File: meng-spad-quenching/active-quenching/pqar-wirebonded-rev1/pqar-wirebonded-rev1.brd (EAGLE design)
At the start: 46 x 46 mm, 47 parts, among them IC1 NL17SZ125, IC14 LTC1711, IC17 NL17SZ125, IC2 LTC1711, IC20 NC7WZ16P6X, IC24 TLV272DGK, IC3 NC7SV74K8X, T1 MMBTH10−4LT1G, U1 SN74LVC1G123DCUT, X1 V_A, X2 OUT, X3 V_LOGIC, X4 I_HOLDOFF

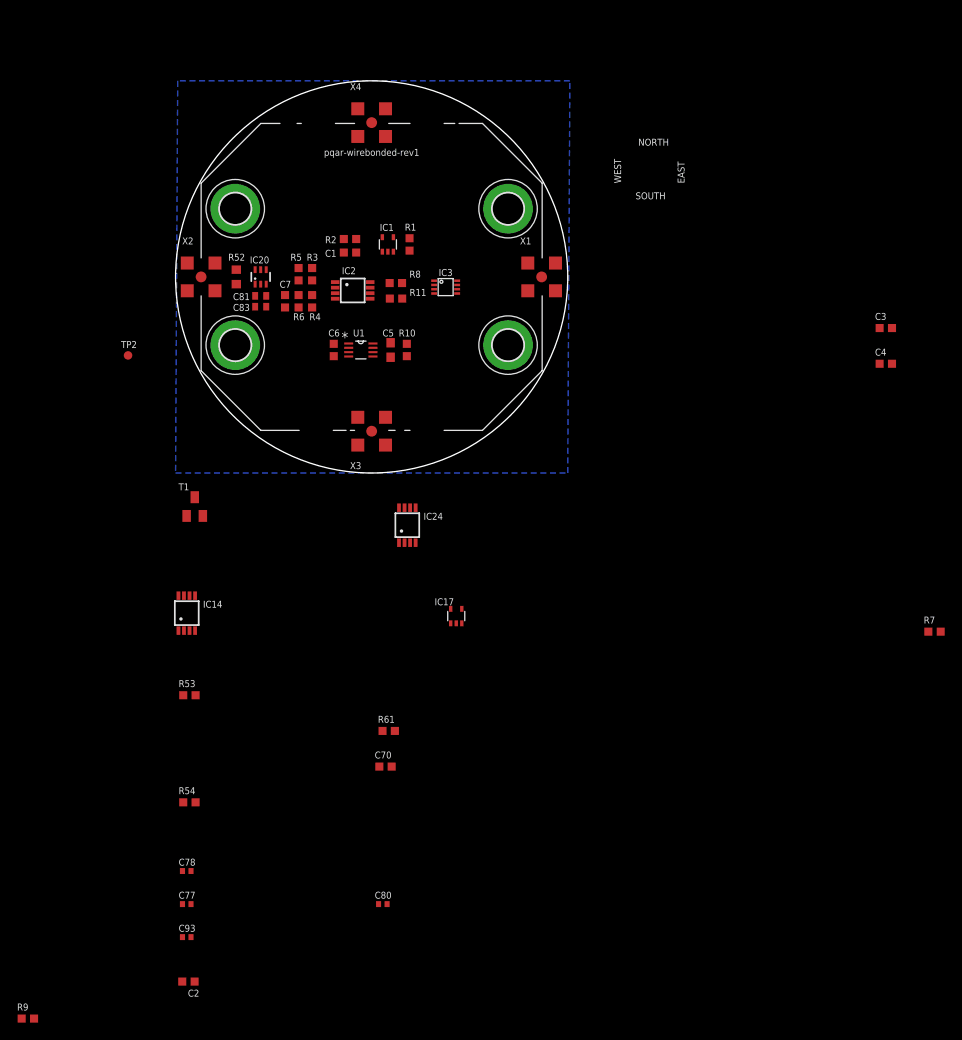
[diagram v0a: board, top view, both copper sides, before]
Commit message: got everything to initially fit on the board
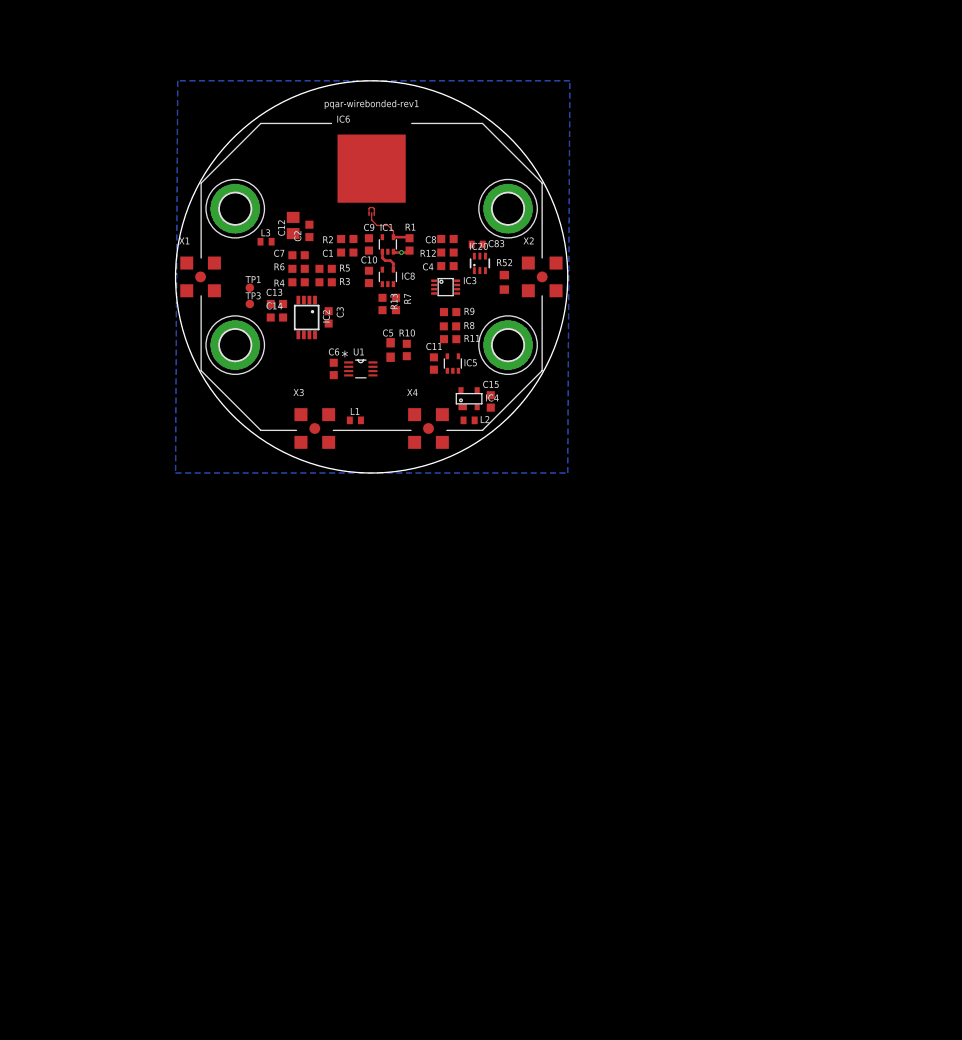
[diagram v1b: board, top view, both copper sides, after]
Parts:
- removed C70: CAP CER 100PF 50V C0G 0603 5%, rcl-modified-footprints:C0603
- removed C77, C80, C93: CAP CER 0.1UF 10V X7R 0402 10%, rcl-modified-footprints:C0402
- removed C78: CAP CER 10000PF 10V X7R 0402 10%, rcl-modified-footprints:C0402
- removed C81: CAP CER 10000PF 10V X7R 0402 10%, rcl:C0402
- removed IC14: LTC1711, meng:MSOP8
- removed IC17: NL17SZ125, 74xx-little-de:SC70-5
- removed IC24: TLV272DGK, meng:MSOP8
- removed R53, R61: RES SMD 220K OHM 1% 1/10W 0603, rcl-modified-footprints:R0603
- removed R54: RES SMD 10K OHM 1% 1/10W 0603, rcl-modified-footprints:R0603
- removed T1: MMBTH10−4LT1G, transistor:SOT23-BEC
- removed TP2: AV_DET, testpad:TP10R
- added C10, C11, C9: IPDiA 935131425610, rcl-modified-footprints:C0603
- added C12: CAP CER 0.1UF 50V X7R 0805 5%, rcl-modified-footprints:C0805
- added C13, C14, C8: DNP, rcl-modified-footprints:C0603
- added C15: CAP CER 0.1UF 50V X7R 0603 5%, rcl-modified-footprints:C0603
- added IC4: BCV62, meng:SOT143B
- added IC5: 74AHC1G14DCK, 74xx-little-us:SC70-5
- added IC6: SPAD-GENERIC, meng:SPAD-WIREBOND-GENERIC-CRYO
- added IC8: 74LVC1G02DCK, 74xx-little-us:SC70-5
- added L1, L2, L3: Samsung CIM05J152NC, meng:R0402
- added R12, R13: RES SMD 0R 0603, rcl-modified-footprints:R0603
- added TP1, TP3: AV_DET, testpad:TP10R
- C2: value CAP CER 100PF 50V C0G 0603 5% -> CAP CER 0.1UF 50V X7R 0603 5%
- R11: value DNP -> RES SMD 0R 0603
- R7: value Vishay FC0603E50R0BTBST1 -> DNP
- moved R9 96.5 mm to (9.21, -4.13)
- moved C2 89.2 mm to (-7.30, 5.40), turned to 90 degrees
- moved R7 73.9 mm to (2.86, -3.17), turned to 270 degrees
- moved C3 65.4 mm to (-5.04, -4.75), turned to 270 degrees
- moved C4 52.7 mm to (8.89, 1.27), turned to 180 degrees
- moved X2 40.0 mm to (20.0, 0.00)
- moved X1 40.0 mm to (-20.1, 0.00)
- moved X4 36.5 mm to (6.67, -17.8)
- moved R52 31.4 mm to (15.6, -0.64)
- moved C83 26.4 mm to (12.4, 3.81), turned to 180 degrees
- moved IC20 25.8 mm to (12.7, 1.59)
- moved R8 8.13 mm to (9.19, -5.80)
- moved R11 7.94 mm to (9.21, -7.30)
- moved X3 6.68 mm to (-6.67, -17.8)
- moved IC2 6.26 mm to (-7.62, -4.76), turned to 180 degrees
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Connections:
- removed net CAP_!RESET: IC17.1
- removed net N$1: C7.1, IC2.2, R5.2, R6.1
- removed net N$11: IC14.3
- removed net N$12: IC20.1, IC20.3, R11.2, U1.5
- removed net N$15: IC14.4
- removed net N$3: C2.1, R2.1, X1.S
- removed net N$4: C1.2, IC2.3, R3.2, R4.1
- removed net N$6: IC3.1, R8.2, R9.2
- removed net NC_RESET: IC3.5
- removed net ONE_SHOT_CAP: C70.1, IC14.2, IC17.4, T1.C
- removed net ONE_SHOT_FB: R53.1, R54.1, T1.E
- removed net ONE_SHOT_VGND: IC24.2, R53.2, R61.1
- removed net PP_N5V0_ANALOG: C80.1, IC24.4, R54.2
- removed net PP_P5V0_ANALOG: C77.1, C78.1, C93.1, IC14.1, IC24.8
- removed net VCC: IC1.5, IC17.5
- removed net VREF_ONE_SHOT_CCS: R61.2
- new net !EN_DRIVER: IC1.1, IC8.4
- new net !QUENCH: IC5.4, R11.2
- new net AV_DET_REF: C13.1, C7.1, IC2.2, R5.2, R6.1
- new net CLK_RESET: IC3.1, R11.1, R8.2, R9.2
- new net DRIVER_IN: IC1.2, IC8.1, R13.1, R7.1
- new net KATHODE_C: C1.2, C14.1, IC2.3, R3.2, R4.1
- new net N$7: C8.1, IC3.6, R12.2
- new net N$8: L2.1, X4.S
- new net QUENCH: IC20.1, IC20.3, IC5.2, R13.2, U1.5
- new net RESET: IC3.5, IC8.2
- new net V_A: L3.1, X1.S
- new net V_A_FILT: C12.1, C2.1, L3.2, R2.1
- net !AV_DET: now also C14.2, TP3.TP
- net !RESET: now also R12.1; no longer IC1.1, IC3.6
- net +5V: now also C10.1, C11.1, C9.1, IC1.5, IC4.3, IC4.4, IC5.5, IC8.5, L1.2; no longer C81.1, IC17.2, X3.S
- net ANODE: now also IC6.A
- net AV_DET: now also C13.2, TP1.TP; no longer TP2.TP
- net GND: now also C10.2, C11.2, C12.2, C15.2, C8.2, C9.2, IC5.3, IC6.GND, IC8.3, R7.2; no longer C70.2, C77.2, C78.2, C80.2, C81.2, C93.2, IC1.2, IC14.5, IC14.6, IC17.3, IC24.3
- net KATHODE: now also IC6.K1, IC6.K2
- net N$17: now also IC4.2
- net N$2: now also C15.1, IC4.1, L2.2; no longer X4.S
- net N$5: now also L1.1, X3.S; no longer IC24.1, T1.B
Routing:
- net ANODE: track 0.00 -> 6.45 mm
- net !EN_DRIVER: track 0.00 -> 3.02 mm
- net GND: track 0.00 -> 2.03 mm, vias 0 -> 1
- net KATHODE: track 0.00 -> 2.00 mm
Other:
- board text removed: "EAST"
- board text removed: "NORTH"
- board text removed: "SOUTH"
- board text removed: "WEST"

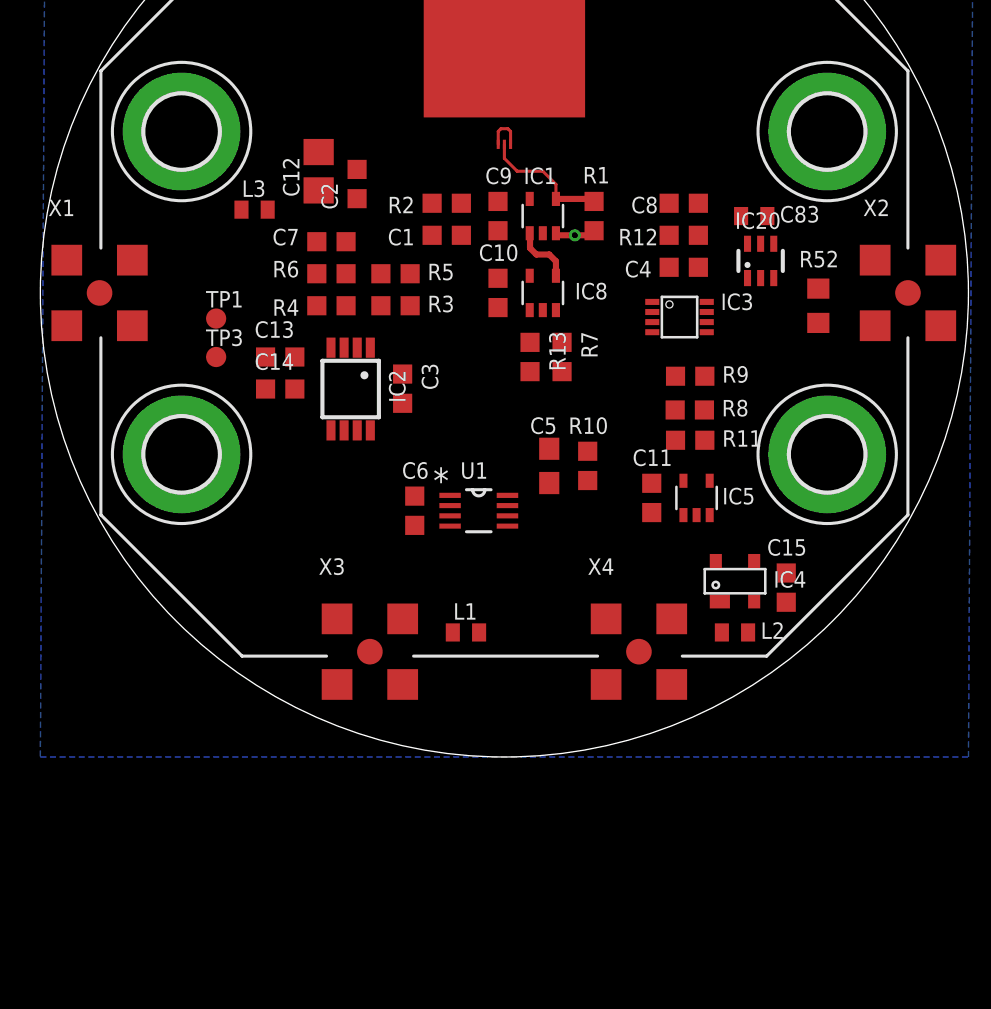
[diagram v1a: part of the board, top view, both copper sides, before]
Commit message: More routing, add or gate for forcing quenching
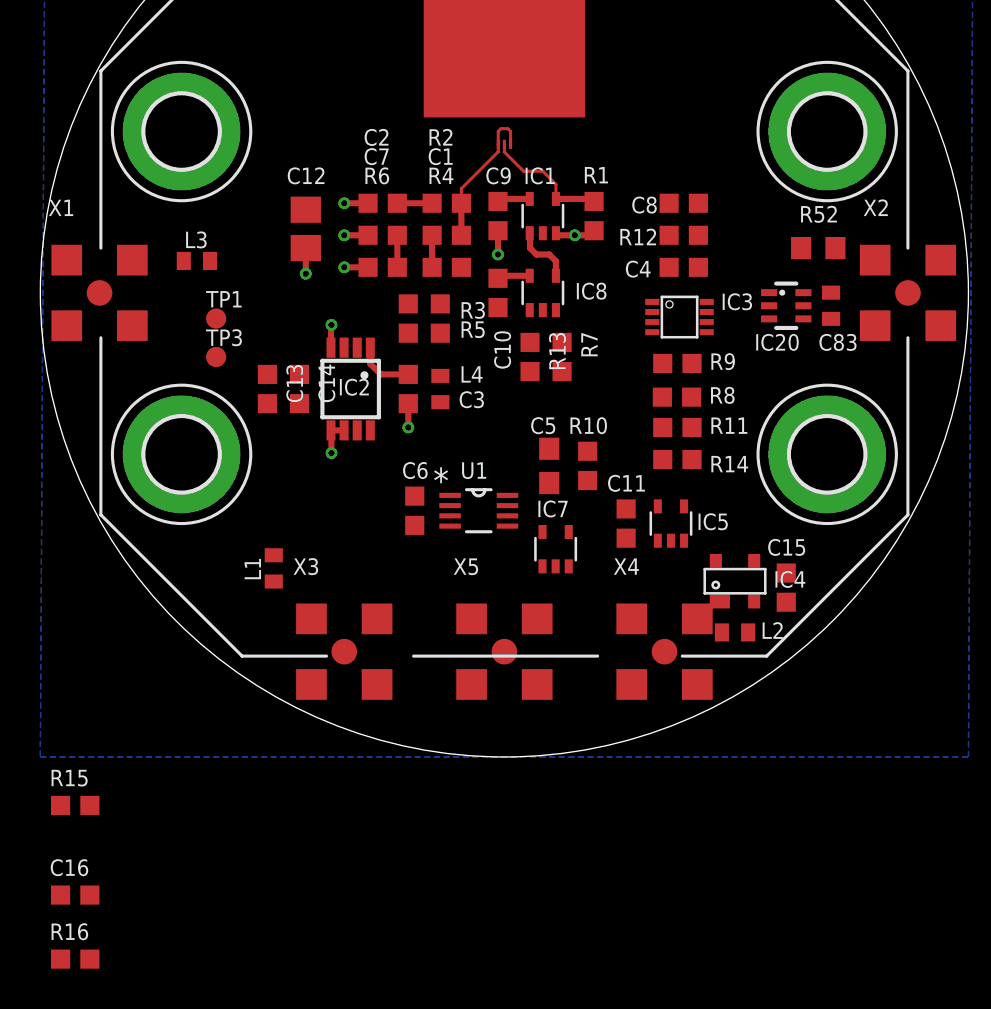
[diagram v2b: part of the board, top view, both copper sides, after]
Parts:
- added C16: IPDiA 935131425610, rcl-modified-footprints:C0603
- added IC7: 74AUC1G32DCK, 74xx-little-us:SC70-5
- added L4: Samsung CIM05J152NC, meng:R0402
- added R14, R15, R16: DNP, rcl-modified-footprints:R0603
- added X5: FORCE_QUENCH, meng:MMCX-SMT-BIGPADS
- moved L1 10.0 mm to (-11.4, -13.7), turned to 90 degrees
- moved R4 6.02 mm to (-2.86, 1.27), turned to 0 degrees
- moved C83 5.85 mm to (16.2, -0.64), turned to 90 degrees
- moved L3 3.82 mm to (-15.2, 1.59)
- moved C12 2.93 mm to (-9.84, 3.17), turned to 270 degrees
- moved R52 2.86 mm to (15.6, 2.22), turned to 180 degrees
- moved IC20 2.56 mm to (14.0, -0.64), turned to 270 degrees
- moved C7 2.56 mm to (-6.03, 2.86)
- moved R6 2.56 mm to (-6.03, 1.27)
- moved R3 2.31 mm to (-3.17, -1.27), turned to 90 degrees
- moved R5 2.31 mm to (-4.76, -1.27), turned to 90 degrees
- moved C11 1.80 mm to (6.03, -11.4)
- moved IC5 1.80 mm to (8.26, -11.4)
- moved C13 1.71 mm to (-11.7, -4.76), turned to 270 degrees
- moved C2 1.59 mm to (-6.03, 4.45), turned to 180 degrees
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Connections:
- net N$17 renamed HOLDOFF_CAP
- net N$2 renamed I_HOLDOFF_FILT
- net N$29 renamed OUT
- net N$7 renamed !RESET_RC
- net N$8 renamed I_HOLDOFF
- net PHOTON_COUNT_OUT renamed OUT_R
- new net FORCE_QUENCH: IC7.2, R15.1, X5.S
- new net HOLDOFF_TIMER: IC20.1, IC20.3, IC7.1, R16.2, U1.5
- new net VDD_COMP: C3.1, IC2.1, L4.2, R3.1, R5.1
- net +5V: now also C16.1, IC7.5, L4.1; no longer C3.1, IC2.1, R3.1, R5.1
- net CLK_RESET: now also R14.1
- net GND: now also C16.2, IC7.3, R15.2, X5.G1, X5.G2, X5.G3, X5.G4
- net QUENCH: now also IC7.4, R14.2, R16.1; no longer IC20.1, IC20.3, U1.5
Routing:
- net GND: track 2.03 -> 12.1 mm, vias 1 -> 9
- net KATHODE: track 2.00 -> 7.27 mm
- net +5V: track 0.00 -> 3.25 mm
- net VDD_COMP: track 0.00 -> 2.90 mm
- net V_A_FILT: track 0.00 -> 1.73 mm
- net KATHODE_C: track 0.00 -> 1.59 mm
- net AV_DET_REF: track 0.00 -> 1.59 mm

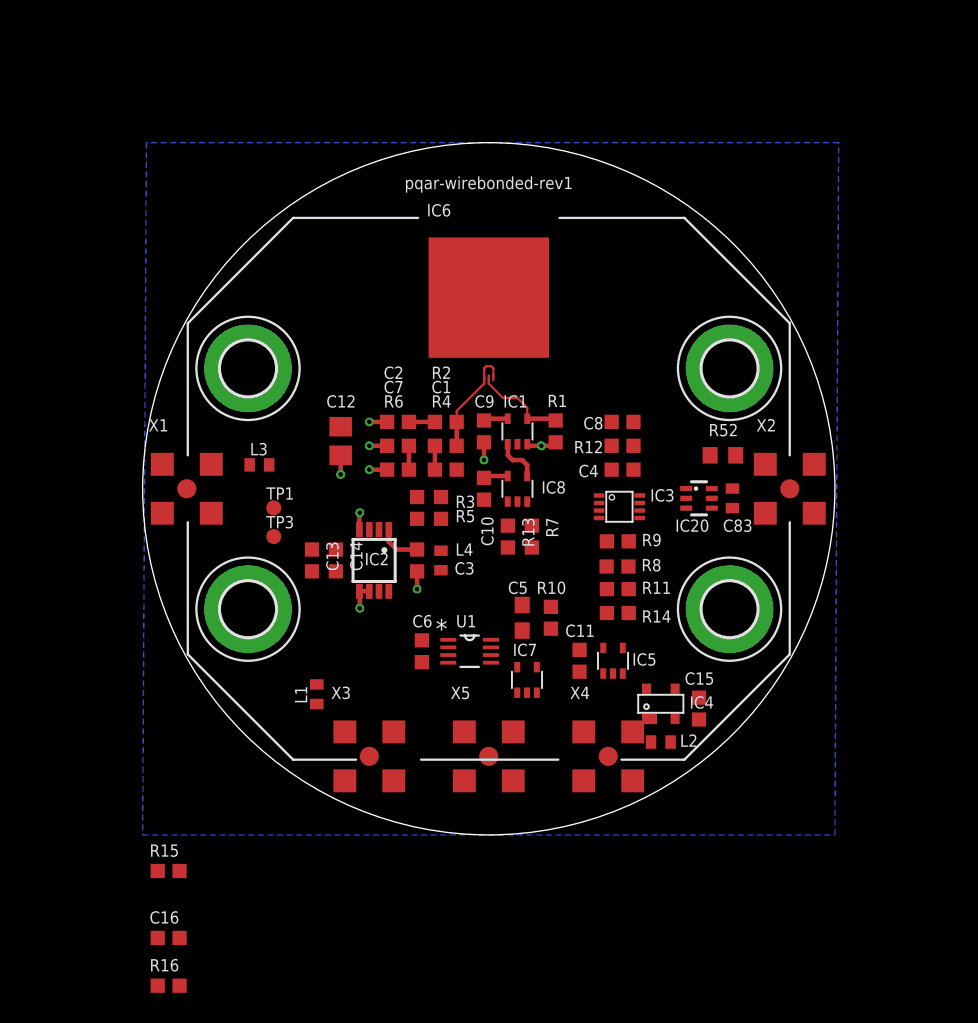
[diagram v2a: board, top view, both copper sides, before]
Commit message: first pass routing done, DRC not clean
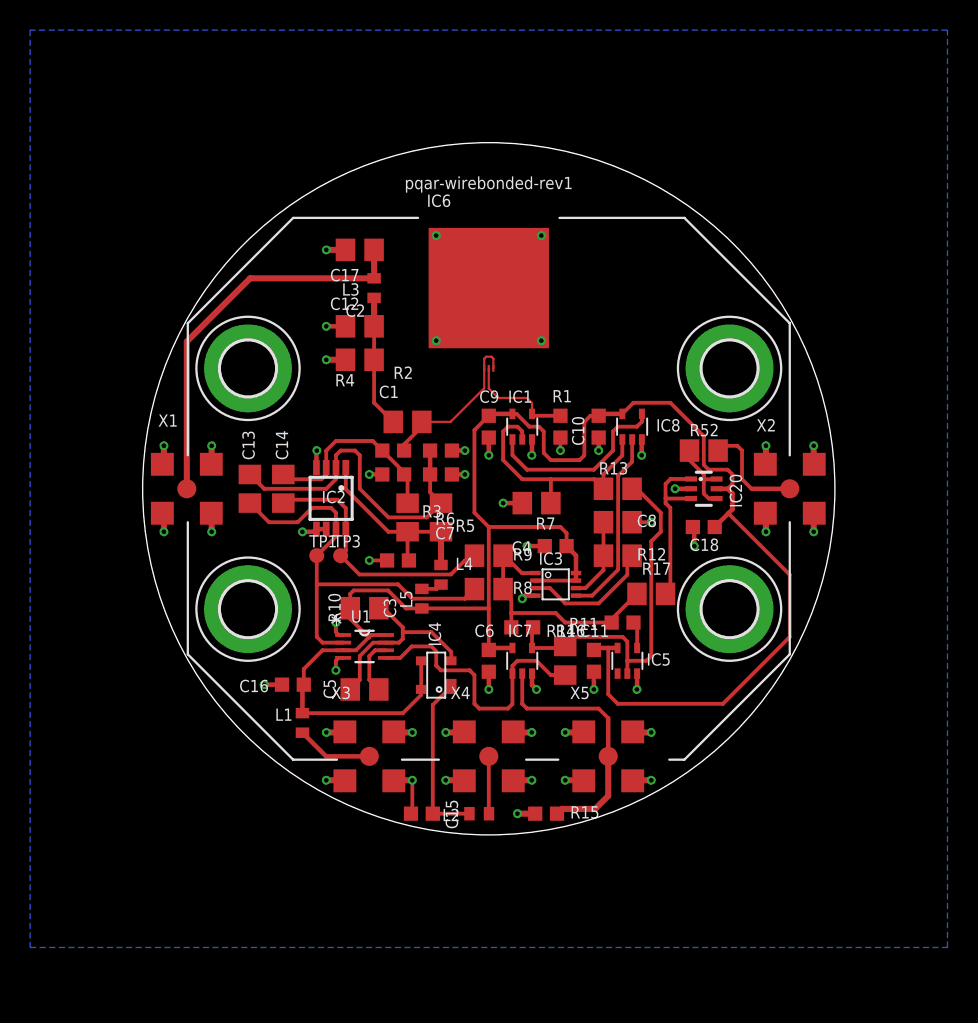
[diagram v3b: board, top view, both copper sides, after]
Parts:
- removed C83: CAP CER 0.1UF 10V X7R 0402 10%, rcl:C0402
- added C17: CAP CER 0.1UF 50V X7R 0805 5%, rcl-modified-footprints:C0805
- added C18: CAP CER 0.1UF 50V X7R 0603 5%, rcl-modified-footprints:C0603
- added L5: Samsung CIM05J152NC, meng:R0402
- added R17: RES SMD 0R 0805, rcl-modified-footprints:R0805
- C13, C14, C8: device rcl-modified-footprints:C0603 -> rcl-modified-footprints:C0805
- C2: value CAP CER 0.1UF 50V X7R 0603 5% -> CAP CER 0.1UF 50V X7R 0805 5%; device rcl-modified-footprints:C0603 -> rcl-modified-footprints:C0805
- C5: value CAP CER 0.1UF 50V X7R 0805 10% -> CAP CER 0.1UF 50V X7R 0805 5%; device rcl:C0603 -> rcl-modified-footprints:C0805
- IC6: value SPAD-GENERIC -> SPAD
- R10, R16, R7, R8, R9: device rcl-modified-footprints:R0603 -> rcl-modified-footprints:R0805
- R12, R13: value RES SMD 0R 0603 -> RES SMD 0R 0805; device rcl-modified-footprints:R0603 -> rcl-modified-footprints:R0805
- R15: value DNP -> RES SMD 10K OHM 1% 1/10W 0603
- R2, R3, R5: value RES SMD 1K OHM 1% 1/10W 0603 -> RES SMD 1K OHM 1% 1/10W 0805; device rcl-modified-footprints:R0603 -> rcl-modified-footprints:R0805
- R52: value RES SMD 49.9 OHM 1% 1/10W 0603 -> RES SMD 49.9 OHM 1% 1/10W 0805; device rcl:R0603 -> rcl:R0805
- moved R16 34.1 mm to (5.08, -11.4), turned to 270 degrees
- moved R15 25.4 mm to (3.81, -21.6), turned to 180 degrees
- moved C15 19.7 mm to (-4.45, -21.6), turned to 180 degrees
- moved C16 18.7 mm to (-13.0, -13.0), turned to 180 degrees
- moved IC4 15.0 mm to (-3.49, -12.4), turned to 90 degrees
- moved L3 14.0 mm to (-7.62, 13.3), turned to 270 degrees
- moved L2 13.0 mm to (-0.64, -21.6), turned to 180 degrees
- moved R10 12.4 mm to (-8.26, -7.94), turned to 0 degrees
- moved C5 11.5 mm to (-8.26, -13.3), turned to 0 degrees
- moved R8 8.69 mm to (0.00, -6.67)
- moved C10 8.67 mm to (7.30, 4.13)
- moved IC8 8.67 mm to (9.53, 4.13)
- moved R9 8.63 mm to (0.00, -4.45)
- moved R13 7.96 mm to (8.57, 0.00), turned to 0 degrees
- moved X4 7.94 mm to (0.00, -17.8)
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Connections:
- net N$16 renamed CEXT
- net N$5 renamed V_LOGIC
- new net N$1: L4.1, L5.2
- new net N$2: IC20.1, IC20.3, R17.2
- net +5V: now also C18.1, L5.1; no longer C83.1, L4.1
- net CLK_RESET: now also R17.1
- net GND: now also C17.2, C18.2; no longer C83.2
- net HOLDOFF_TIMER: no longer IC20.1, IC20.3
- net V_A: now also C17.1
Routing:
- net +5V: track 3.25 -> 121.2 mm
- net GND: track 12.1 -> 64.0 mm, vias 9 -> 52
- net AV_DET: track 0.00 -> 28.6 mm
- net V_A: track 0.00 -> 25.9 mm
- net QUENCH: track 0.00 -> 24.5 mm
- net AV_DET_REF: track 1.59 -> 22.4 mm
- net HOLDOFF_TIMER: track 0.00 -> 18.8 mm
- net !AV_DET: track 0.00 -> 17.7 mm
- net FORCE_QUENCH: track 0.00 -> 17.2 mm
- net CLK_RESET: track 0.00 -> 17.1 mm
- net DRIVER_IN: track 0.00 -> 17.1 mm
- net HOLDOFF_CAP: track 0.00 -> 13.1 mm
- net RESET: track 0.00 -> 12.6 mm
- net KATHODE_C: track 1.59 -> 13.3 mm
- net I_HOLDOFF_FILT: track 0.00 -> 11.4 mm
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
